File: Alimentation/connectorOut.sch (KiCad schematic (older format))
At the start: 2 parts

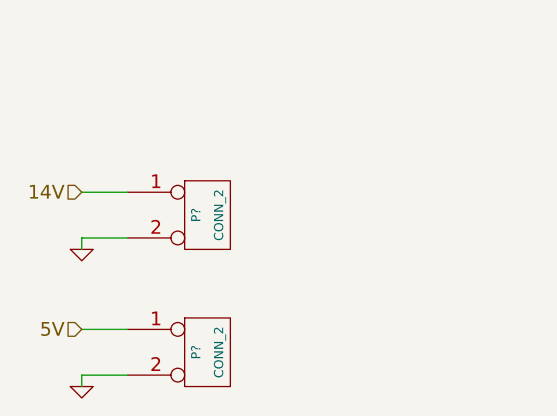
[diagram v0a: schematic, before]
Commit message: Adding board for alimentation
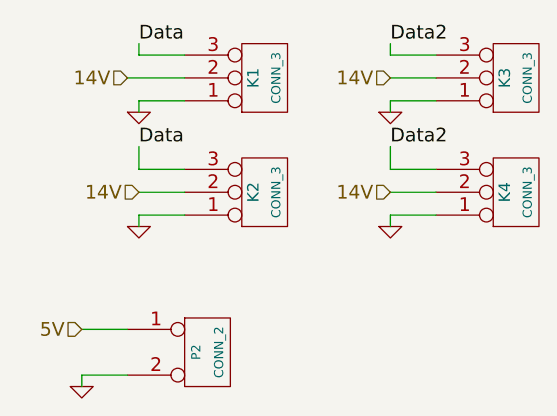
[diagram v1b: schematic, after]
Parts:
- removed P?: CONN_2, symbol CONN_2
- added K1, K2, K3, K4: CONN_3, symbol CONN_3
- gave numbers to parts that had none: 1
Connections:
- net 14V: now also K1.2 (PM), K2.2 (PM), K3.2 (PM), K4.2 (PM)
- net GND: now also K1.1 (P1), K2.1 (P1), K3.1 (P1), K4.1 (P1)
- new net Data: K1.3 (P3), K2.3 (P3)
- new net Data2: K3.3 (P3), K4.3 (P3)
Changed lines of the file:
@@
-EESchema Schematic File Version 2  date Thu 13 Mar 2014 12:12:56 CET
+EESchema Schematic File Version 2
 LIBS:power
 LIBS:device
@@
 LIBS:perso
 LIBS:alimentation-cache
-EELAYER 25  0
+EELAYER 24 0
 EELAYER END
-$Descr A4 11700 8267
+$Descr A4 11693 8268
 encoding utf-8
-Sheet 2 7
+Sheet 2 5
 Title ""
-Date "13 mar 2014"
+Date "20 mar 2014"
 Rev ""
 Comp ""
@@
 Comment4 ""
 $EndDescr
-Text HLabel 3250 2450 0    60   Input ~ 0
+Text HLabel 3500 2450 0    60   Input ~ 0
 14V
 Text HLabel 3250 3050 0    60   Input ~ 0
 5V
 $Comp
-L GND #PWR?
+L GND #PWR01
 U 1 1 53147F6C
 P 3250 3300
-F 0 "#PWR?" H 3250 3300 30  0001 C CNN
+F 0 "#PWR01" H 3250 3300 30  0001 C CNN
 F 1 "GND" H 3250 3230 30  0001 C CNN
+F 2 "" H 3250 3300 60  0001 C CNN
+F 3 "" H 3250 3300 60  0001 C CNN
 	1    3250 3300
 	1    0    0    -1
 $EndComp
 $Comp
-L GND #PWR?
+L GND #PWR02
 U 1 1 53147F69
-P 3250 2700
-F 0 "#PWR?" H 3250 2700 30  0001 C CNN
-F 1 "GND" H 3250 2630 30  0001 C CNN
-	1    3250 2700
+P 3500 2600
+F 0 "#PWR02" H 3500 2600 30  0001 C CNN
+F 1 "GND" H 3500 2530 30  0001 C CNN
+F 2 "" H 3500 2600 60  0001 C CNN
+F 3 "" H 3500 2600 60  0001 C CNN
+	1    3500 2600
 	1    0    0    -1
 $EndComp
@@
 	3250 3250 3450 3250
 Wire Wire Line
-	3250 2700 3250 2650
-Wire Wire Line
-	3250 2650 3450 2650
-Wire Wire Line
-	3450 2450 3250 2450
+	3500 2600 3500 2550
+Wire Wire Line
+	3500 2550 3700 2550
+Wire Wire Line
+	3700 2450 3500 2450
 Wire Wire Line
 	3450 3050 3250 3050
 $Comp
-L CONN_2 P?
+L CONN_2 P2
 U 1 1 53147F3D
 P 3800 3150
-F 0 "P?" V 3750 3150 40  0000 C CNN
+F 0 "P2" V 3750 3150 40  0000 C CNN
 F 1 "CONN_2" V 3850 3150 40  0000 C CNN
+F 2 "" H 3800 3150 60  0001 C CNN
+F 3 "" H 3800 3150 60  0001 C CNN
 	1    3800 3150
 	1    0    0    -1
 $EndComp
 $Comp
-L CONN_2 P?
-U 1 1 53147F38
-P 3800 2550
-F 0 "P?" V 3750 2550 40  0000 C CNN
-F 1 "CONN_2" V 3850 2550 40  0000 C CNN
-	1    3800 2550
-	1    0    0    -1
-$EndComp
+L CONN_3 K2
+U 1 1 5357B23F
+P 4050 2450
+F 0 "K2" V 4000 2450 50  0000 C CNN
+F 1 "CONN_3" V 4100 2450 40  0000 C CNN
+F 2 "" H 4050 2450 60  0000 C CNN
+F 3 "" H 4050 2450 60  0000 C CNN
+	1    4050 2450
+	1    0    0    1
+$EndComp
+$Comp
+L CONN_3 K1
+U 1 1 5357B24C
+P 4050 1950
+F 0 "K1" V 4000 1950 50  0000 C CNN
+F 1 "CONN_3" V 4100 1950 40  0000 C CNN
+F 2 "" H 4050 1950 60  0000 C CNN
+F 3 "" H 4050 1950 60  0000 C CNN
+	1    4050 1950
+	1    0    0    1
+$EndComp
+Wire Wire Line
+	3700 2350 3500 2350
+Wire Wire Line
+	3500 2350 3500 2250
+Text Label 3500 2250 0    60   ~ 0
+Data
+$Comp
+L GND #PWR03
+U 1 1 5357B2DE
+P 3500 2100
+F 0 "#PWR03" H 3500 2100 30  0001 C CNN
+F 1 "GND" H 3500 2030 30  0001 C CNN
+F 2 "" H 3500 2100 60  0001 C CNN
+F 3 "" H 3500 2100 60  0001 C CNN
+	1    3500 2100
+	1    0    0    -1
+$EndComp
+Wire Wire Line
+	3700 2050 3500 2050
+Wire Wire Line
+	3500 2050 3500 2100
+Wire Wire Line
+	3700 1850 3500 1850
+Wire Wire Line
+	3500 1850 3500 1800
+Text Label 3500 1800 0    60   ~ 0
+Data
+Text HLabel 4600 2450 0    60   Input ~ 0
+14V
+$Comp
+L GND #PWR04
+U 1 1 5357B2FD
+P 4600 2600
+F 0 "#PWR04" H 4600 2600 30  0001 C CNN
+F 1 "GND" H 4600 2530 30  0001 C CNN
+F 2 "" H 4600 2600 60  0001 C CNN
+F 3 "" H 4600 2600 60  0001 C CNN
+	1    4600 2600
+	1    0    0    -1
+$EndComp
+Wire Wire Line
+	4600 2600 4600 2550
+Wire Wire Line
+	4600 2550 4800 2550
+Wire Wire Line
+	4800 2450 4600 2450
+$Comp
+L CONN_3 K4
+U 1 1 5357B306
+P 5150 2450
+F 0 "K4" V 5100 2450 50  0000 C CNN
+F 1 "CONN_3" V 5200 2450 40  0000 C CNN
+F 2 "" H 5150 2450 60  0000 C CNN
+F 3 "" H 5150 2450 60  0000 C CNN
+	1    5150 2450
+	1    0    0    1
+$EndComp
+$Comp
+L CONN_3 K3
+U 1 1 5357B30C
+P 5150 1950
+F 0 "K3" V 5100 1950 50  0000 C CNN
+F 1 "CONN_3" V 5200 1950 40  0000 C CNN
+F 2 "" H 5150 1950 60  0000 C CNN
+F 3 "" H 5150 1950 60  0000 C CNN
+	1    5150 1950
+	1    0    0    1
+$EndComp
+Wire Wire Line
+	4800 2350 4600 2350
+Wire Wire Line
+	4600 2350 4600 2250
+Text Label 4600 2250 0    60   ~ 0
+Data2
+$Comp
+L GND #PWR05
+U 1 1 5357B315
+P 4600 2100
+F 0 "#PWR05" H 4600 2100 30  0001 C CNN
+F 1 "GND" H 4600 2030 30  0001 C CNN
+F 2 "" H 4600 2100 60  0001 C CNN
+F 3 "" H 4600 2100 60  0001 C CNN
+	1    4600 2100
+	1    0    0    -1
+$EndComp
+Wire Wire Line
+	4800 2050 4600 2050
+Wire Wire Line
+	4600 2050 4600 2100
+Wire Wire Line
+	4800 1850 4600 1850
+Wire Wire Line
+	4600 1850 4600 1800
+Text Label 4600 1800 0    60   ~ 0
+Data2
+Text HLabel 4600 1950 0    60   Input ~ 0
+14V
+Text HLabel 3450 1950 0    60   Input ~ 0
+14V
+Wire Wire Line
+	3450 1950 3700 1950
+Wire Wire Line
+	4600 1950 4800 1950
 $EndSCHEMATC
